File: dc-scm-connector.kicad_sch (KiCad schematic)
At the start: 101 parts, among them J3 PCB-Edge_DC-SCM-2.1_2x84_Rev-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

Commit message: [#100764] Update components on PCB
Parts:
- removed C256, C257, C258, C259, C260, C261, C262, C263, C264, C265, C266, C267: C_100n_0402, antmicro-footprints:C_0402_1005Metric, symbol antmicroCapacitors0402:C_100n_0402
- added C701, C702, C703, C704, C705, C706, C707, C708, C709, C710, C711, C712: C_100n_0402, antmicro-footprints:C_0402_1005Metric, symbol antmicroCapacitors0402:C_100n_0402
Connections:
- net DC-SCM_PCIE_HPMROOT_TX0+ is gone; now on net DC-SCM_PCIE_HPMROOT.TX0+: J3.B31 (PCIE_HPMROOT_HPM_SCM_4_DP)
- net DC-SCM_PCIE_HPMROOT_TX0- is gone; now on net DC-SCM_PCIE_HPMROOT.TX0-: J3.B30 (PCIE_HPMROOT_HPM_SCM_4_DN)
- net DC-SCM_USB_HPMROOT_TX0+ is gone; now on net DC-SCM_PCIE_USB_HPMROOT.TX0+: J3.B66 (PCIE_HPMROOT_HPM_SCM_5_DP)
- net DC-SCM_USB_HPMROOT_TX0- is gone; now on net DC-SCM_PCIE_USB_HPMROOT.TX0-: J3.B65 (PCIE_HPMROOT_HPM_SCM_5_DN)
- net DC_SCM_PCIE_TX0+ is gone; now on net DC_SCM_PCIE.TX0+: J3.OB3 (PCIE_HPMROOT_HPM_SCM_0_DP)
- net DC_SCM_PCIE_TX0- is gone; now on net DC_SCM_PCIE.TX0-: J3.OB2 (PCIE_HPMROOT_HPM_SCM_0_DN)
- net DC_SCM_PCIE_TX1+ is gone; now on net DC_SCM_PCIE.TX1+: J3.OB6 (PCIE_HPMROOT_HPM_SCM_1_DP)
- net DC_SCM_PCIE_TX1- is gone; now on net DC_SCM_PCIE.TX1-: J3.OB5 (PCIE_HPMROOT_HPM_SCM_1_DN)
- net DC_SCM_PCIE_TX2+ is gone; now on net DC_SCM_PCIE.TX2+: J3.OB9 (PCIE_HPMROOT_HPM_SCM_2_DP)
- net DC_SCM_PCIE_TX2- is gone; now on net DC_SCM_PCIE.TX2-: J3.OB8 (PCIE_HPMROOT_HPM_SCM_2_DN)
- net DC_SCM_PCIE_TX3+ is gone; now on net DC_SCM_PCIE.TX3+: J3.OB12 (PCIE_HPMROOT_HPM_SCM_3_DP)
- net DC_SCM_PCIE_TX3- is gone; now on net DC_SCM_PCIE.TX3-: J3.OB11 (PCIE_HPMROOT_HPM_SCM_3_DN)
- net DC-SCM_PCIE_HPMROOT.RX0+: now also C709.1; no longer J3.A31 (PCIE_HPMROOT_SCM_HPM_4_DP)
- net DC-SCM_PCIE_HPMROOT.RX0-: now also C710.1; no longer J3.A30 (PCIE_HPMROOT_SCM_HPM_4_DN)
- net DC-SCM_PCIE_USB_HPMROOT.RX0+: now also C711.1; no longer J3.A66 (PCIE_HPMROOT_SCM_HPM_5_DP)
- net DC-SCM_PCIE_USB_HPMROOT.RX0-: now also C712.1; no longer J3.A65 (PCIE_HPMROOT_SCM_HPM_5_DN)
- net DC_SCM_PCIE.RX0+: now also C701.1; no longer J3.OA3 (PCIE_HPMROOT_SCM_HPM_0_DP)
- net DC_SCM_PCIE.RX0-: now also C702.1; no longer J3.OA2 (PCIE_HPMROOT_SCM_HPM_0_DN)
- net DC_SCM_PCIE.RX1+: now also C703.1; no longer J3.OA6 (PCIE_HPMROOT_SCM_HPM_1_DP)
- net DC_SCM_PCIE.RX1-: now also C704.1; no longer J3.OA5 (PCIE_HPMROOT_SCM_HPM_1_DN)
- net DC_SCM_PCIE.RX2+: now also C705.1; no longer J3.OA9 (PCIE_HPMROOT_SCM_HPM_2_DP)
- net DC_SCM_PCIE.RX2-: now also C706.1; no longer J3.OA8 (PCIE_HPMROOT_SCM_HPM_2_DN)
- net DC_SCM_PCIE.RX3+: now also C707.1; no longer J3.OA12 (PCIE_HPMROOT_SCM_HPM_3_DP)
- net DC_SCM_PCIE.RX3-: now also C708.1; no longer J3.OA11 (PCIE_HPMROOT_SCM_HPM_3_DN)
- new net DC-SCM_PCIE_HPMROOT_RX0+: C709.2, J3.A31 (PCIE_HPMROOT_SCM_HPM_4_DP)
- new net DC-SCM_PCIE_HPMROOT_RX0-: C710.2, J3.A30 (PCIE_HPMROOT_SCM_HPM_4_DN)
- new net DC-SCM_USB_HPMROOT_RX0+: C711.2, J3.A66 (PCIE_HPMROOT_SCM_HPM_5_DP)
- new net DC-SCM_USB_HPMROOT_RX0-: C712.2, J3.A65 (PCIE_HPMROOT_SCM_HPM_5_DN)
- new net DC_SCM_PCIE_RX0+: C701.2, J3.OA3 (PCIE_HPMROOT_SCM_HPM_0_DP)
- new net DC_SCM_PCIE_RX0-: C702.2, J3.OA2 (PCIE_HPMROOT_SCM_HPM_0_DN)
- new net DC_SCM_PCIE_RX1+: C703.2, J3.OA6 (PCIE_HPMROOT_SCM_HPM_1_DP)
- new net DC_SCM_PCIE_RX1-: C704.2, J3.OA5 (PCIE_HPMROOT_SCM_HPM_1_DN)
- new net DC_SCM_PCIE_RX2+: C705.2, J3.OA9 (PCIE_HPMROOT_SCM_HPM_2_DP)
- new net DC_SCM_PCIE_RX2-: C706.2, J3.OA8 (PCIE_HPMROOT_SCM_HPM_2_DN)
- new net DC_SCM_PCIE_RX3+: C707.2, J3.OA12 (PCIE_HPMROOT_SCM_HPM_3_DP)
- new net DC_SCM_PCIE_RX3-: C708.2, J3.OA11 (PCIE_HPMROOT_SCM_HPM_3_DN)

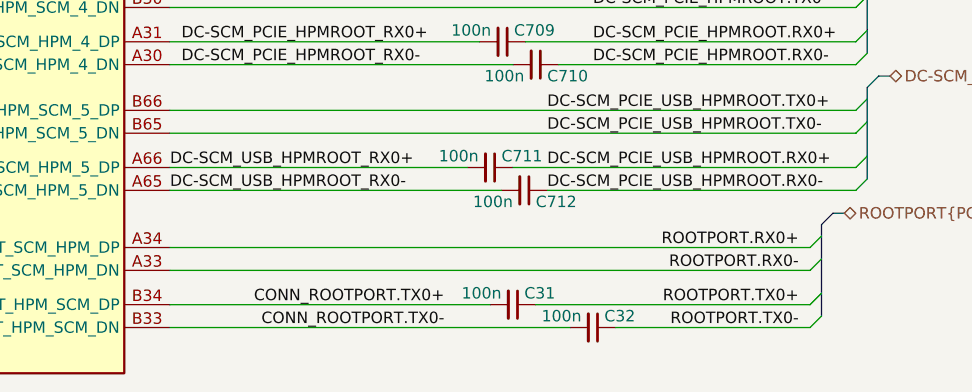
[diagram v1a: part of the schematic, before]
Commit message: [#100764] Move rootport pcie capacitors and add clock labels
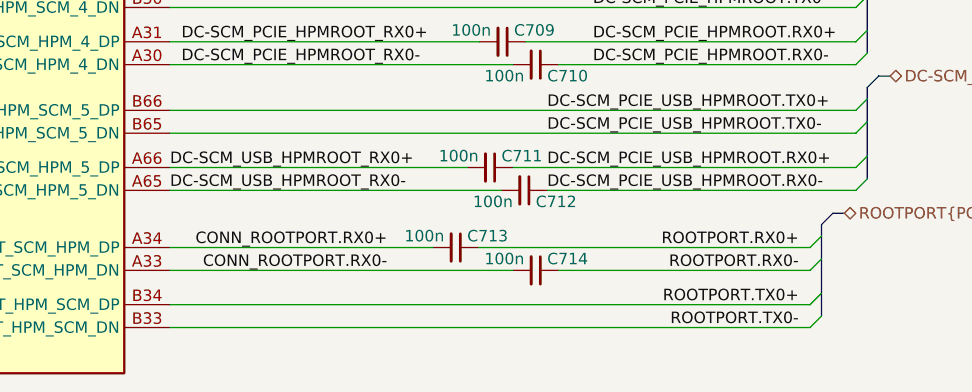
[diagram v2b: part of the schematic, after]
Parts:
- removed C31, C32: C_100n_0402, antmicro-footprints:C_0402_1005Metric, symbol antmicroCapacitors0402:C_100n_0402
- added C713, C714: C_100n_0402, antmicro-footprints:C_0402_1005Metric, symbol antmicroCapacitors0402:C_100n_0402
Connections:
- net CONN_ROOTPORT.TX0+ is gone; now on net ROOTPORT.TX0+: J3.B34 (PCIE_SCMROOT_HPM_SCM_DP)
- net CONN_ROOTPORT.TX0- is gone; now on net ROOTPORT.TX0-: J3.B33 (PCIE_SCMROOT_HPM_SCM_DN)
- net ROOTPORT.RX0+: now also C713.1; no longer J3.A34 (PCIE_SCMROOT_SCM_HPM_DP)
- net ROOTPORT.RX0-: now also C714.1; no longer J3.A33 (PCIE_SCMROOT_SCM_HPM_DN)
- new net CONN_ROOTPORT.RX0+: C713.2, J3.A34 (PCIE_SCMROOT_SCM_HPM_DP)
- new net CONN_ROOTPORT.RX0-: C714.2, J3.A33 (PCIE_SCMROOT_SCM_HPM_DN)

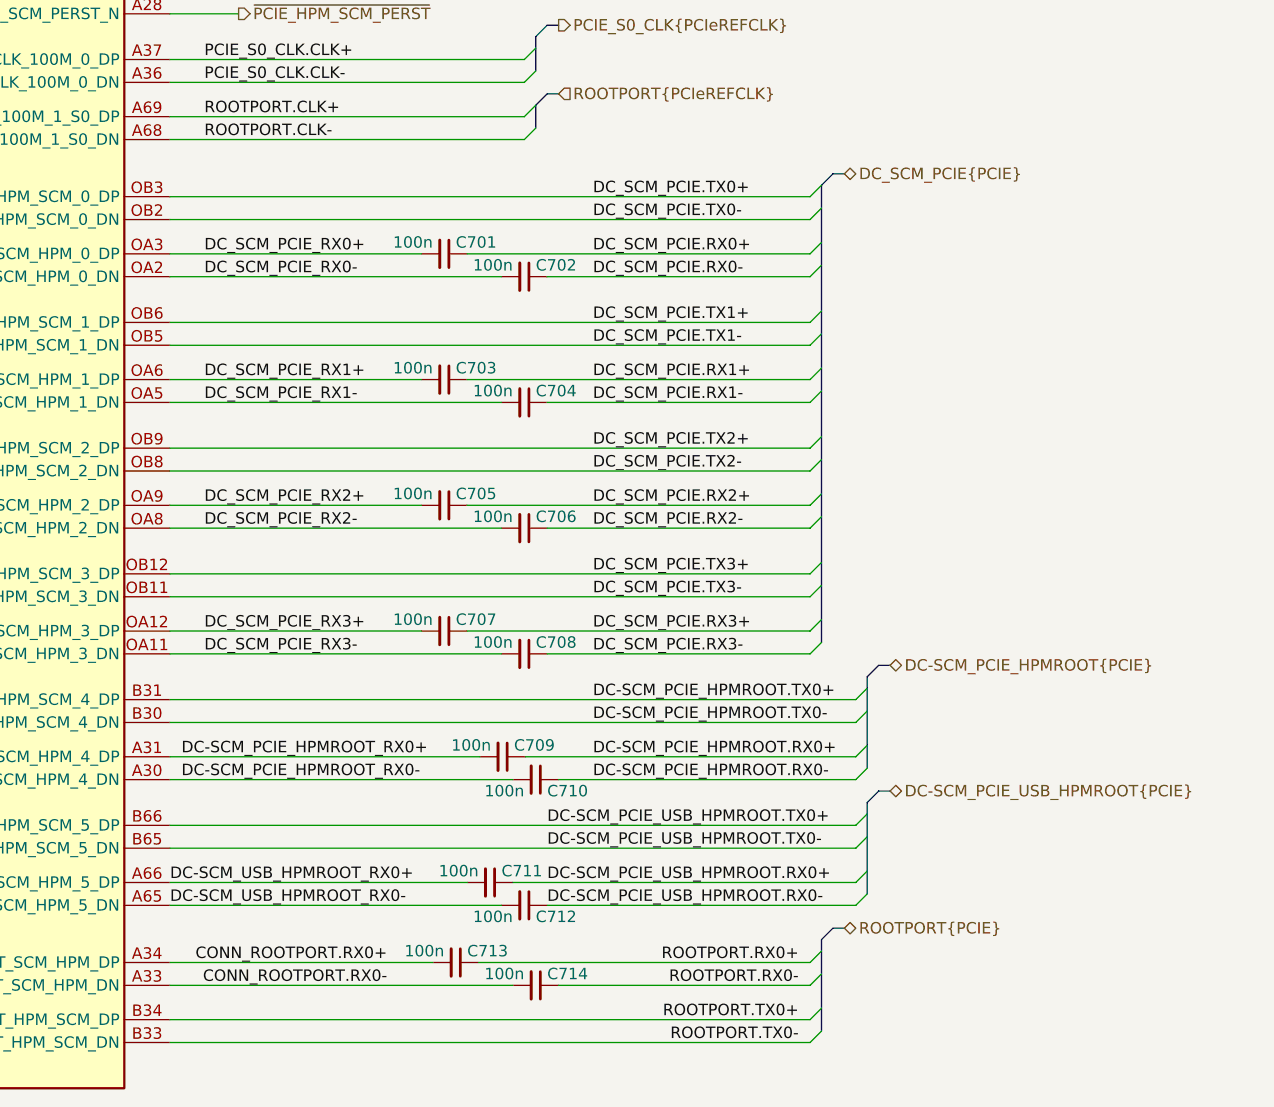
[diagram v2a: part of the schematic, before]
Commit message: [#100707] Move PCIe AC coupling capacitrs on the schematic, close to TX source, add 0Rs to DC-SCM PCIe
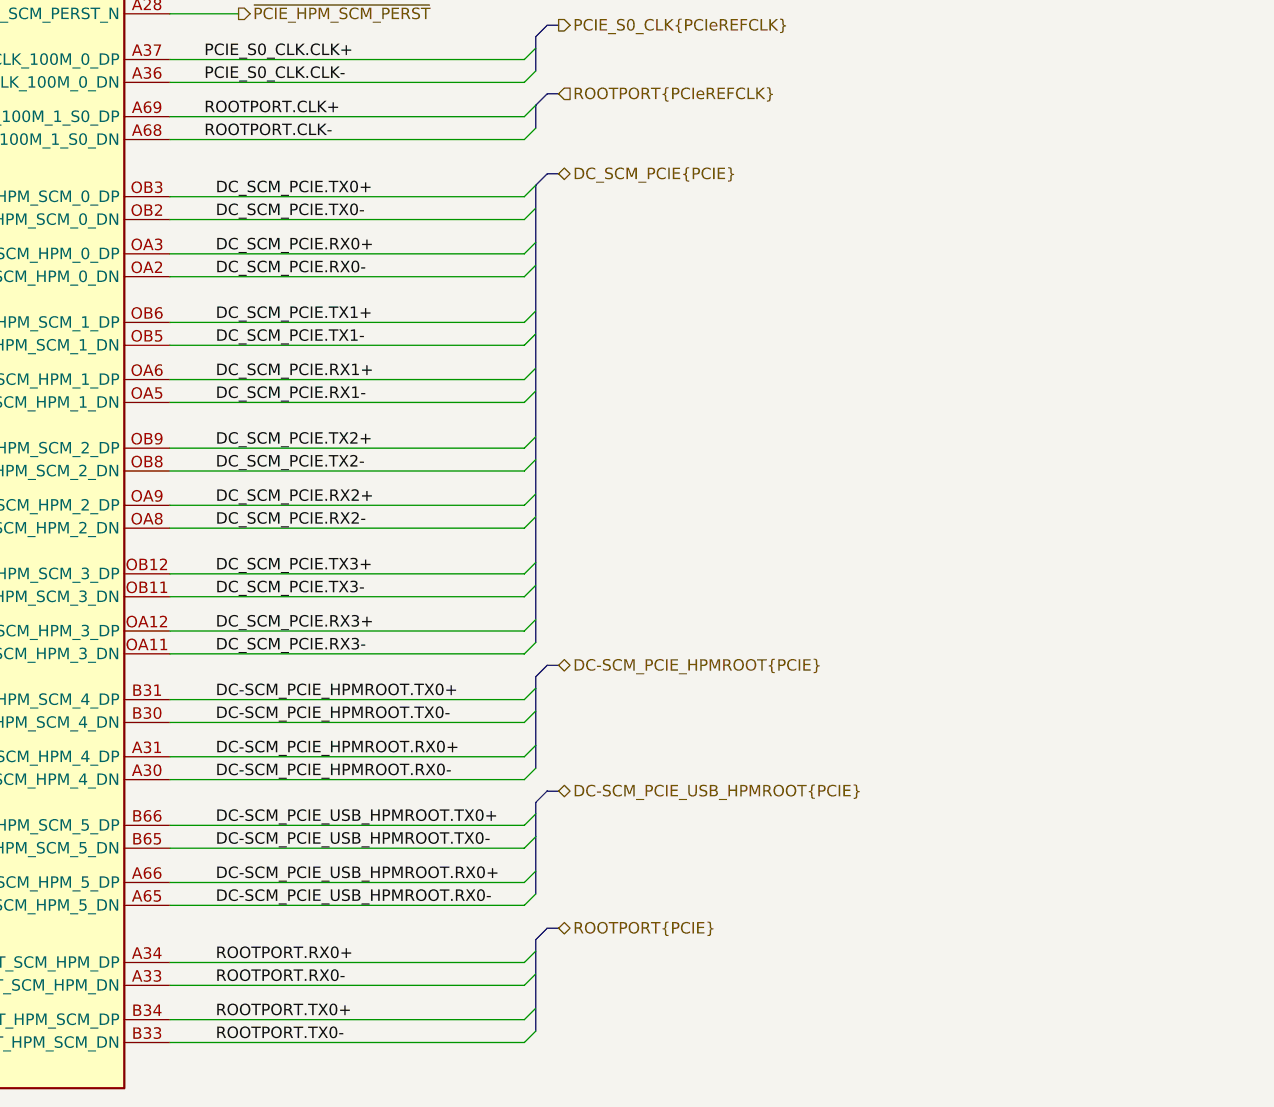
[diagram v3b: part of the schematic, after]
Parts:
- removed C701, C702, C703, C704, C705, C706, C707, C708, C709, C710, C711, C712, C713, C714: C_100n_0402, antmicro-footprints:C_0402_1005Metric, symbol antmicroCapacitors0402:C_100n_0402
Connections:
- net CONN_ROOTPORT.RX0+ is gone; now on net ROOTPORT.RX0+: J3.A34 (PCIE_SCMROOT_SCM_HPM_DP)
- net CONN_ROOTPORT.RX0- is gone; now on net ROOTPORT.RX0-: J3.A33 (PCIE_SCMROOT_SCM_HPM_DN)
- net DC-SCM_PCIE_HPMROOT_RX0+ is gone; now on net DC-SCM_PCIE_HPMROOT.RX0+: J3.A31 (PCIE_HPMROOT_SCM_HPM_4_DP)
- net DC-SCM_PCIE_HPMROOT_RX0- is gone; now on net DC-SCM_PCIE_HPMROOT.RX0-: J3.A30 (PCIE_HPMROOT_SCM_HPM_4_DN)
- net DC-SCM_USB_HPMROOT_RX0+ is gone; now on net DC-SCM_PCIE_USB_HPMROOT.RX0+: J3.A66 (PCIE_HPMROOT_SCM_HPM_5_DP)
- net DC-SCM_USB_HPMROOT_RX0- is gone; now on net DC-SCM_PCIE_USB_HPMROOT.RX0-: J3.A65 (PCIE_HPMROOT_SCM_HPM_5_DN)
- net DC_SCM_PCIE_RX0+ is gone; now on net DC_SCM_PCIE.RX0+: J3.OA3 (PCIE_HPMROOT_SCM_HPM_0_DP)
- net DC_SCM_PCIE_RX0- is gone; now on net DC_SCM_PCIE.RX0-: J3.OA2 (PCIE_HPMROOT_SCM_HPM_0_DN)
- net DC_SCM_PCIE_RX1+ is gone; now on net DC_SCM_PCIE.RX1+: J3.OA6 (PCIE_HPMROOT_SCM_HPM_1_DP)
- net DC_SCM_PCIE_RX1- is gone; now on net DC_SCM_PCIE.RX1-: J3.OA5 (PCIE_HPMROOT_SCM_HPM_1_DN)
- net DC_SCM_PCIE_RX2+ is gone; now on net DC_SCM_PCIE.RX2+: J3.OA9 (PCIE_HPMROOT_SCM_HPM_2_DP)
- net DC_SCM_PCIE_RX2- is gone; now on net DC_SCM_PCIE.RX2-: J3.OA8 (PCIE_HPMROOT_SCM_HPM_2_DN)
- net DC_SCM_PCIE_RX3+ is gone; now on net DC_SCM_PCIE.RX3+: J3.OA12 (PCIE_HPMROOT_SCM_HPM_3_DP)
- net DC_SCM_PCIE_RX3- is gone; now on net DC_SCM_PCIE.RX3-: J3.OA11 (PCIE_HPMROOT_SCM_HPM_3_DN)

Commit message: [#101095] Swap I2C on DC-SCM
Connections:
- net DC_SCM_I2C3.SCL: now also R78.1; no longer R70.1
- net DC_SCM_I2C3.SDA: now also R80.1; no longer R72.1
- net DC_SCM_I2C4.SCL: now also R70.1; no longer R74.1
- net DC_SCM_I2C4.SDA: now also R72.1; no longer R76.1
- net DC_SCM_I2C5.SCL: now also R82.1; no longer R78.1
- net DC_SCM_I2C5.SDA: now also R84.1; no longer R80.1
- net DC_SCM_I2C6.SCL: now also R74.1; no longer R82.1
- net DC_SCM_I2C6.SDA: now also R76.1; no longer R84.1
- net DC_SCM_I2C_I3C13.SCL: now also R75.2; no longer R63.2
- net DC_SCM_I2C_I3C13.SDA: now also R77.2; no longer R65.2
- net DC_SCM_I2C_I3C16.SCL: now also R63.2; no longer R75.2
- net DC_SCM_I2C_I3C16.SDA: now also R65.2; no longer R77.2

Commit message: [#101340] Add flash sockets
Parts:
- added R701, R702, R703: R_10k_0402, antmicro-footprints:R_0402_1005Metric, symbol antmicroResistors0402:R_10k_0402
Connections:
- net DC_SCM_I2C7.SCL: now also R702.1
- net DC_SCM_I2C7.SDA: now also R703.1
- net DC_SCM_P3V0: now also R701.2
- net ~{DC_SCM_INTRUSION}: now also R701.1
- new net +3V3: R702.2, R703.2
